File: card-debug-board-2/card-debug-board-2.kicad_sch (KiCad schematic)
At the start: 30 parts, among them J1 2-1734592-0, J2 Conn_01x05, J5 0676430910, J6 629105150521, SW1 PCM13SMTR, SW2 B3F-1000, SW3 CFS-0103TB, SW4 CFS-0103TB, U1 MIC5205-3.3YM5

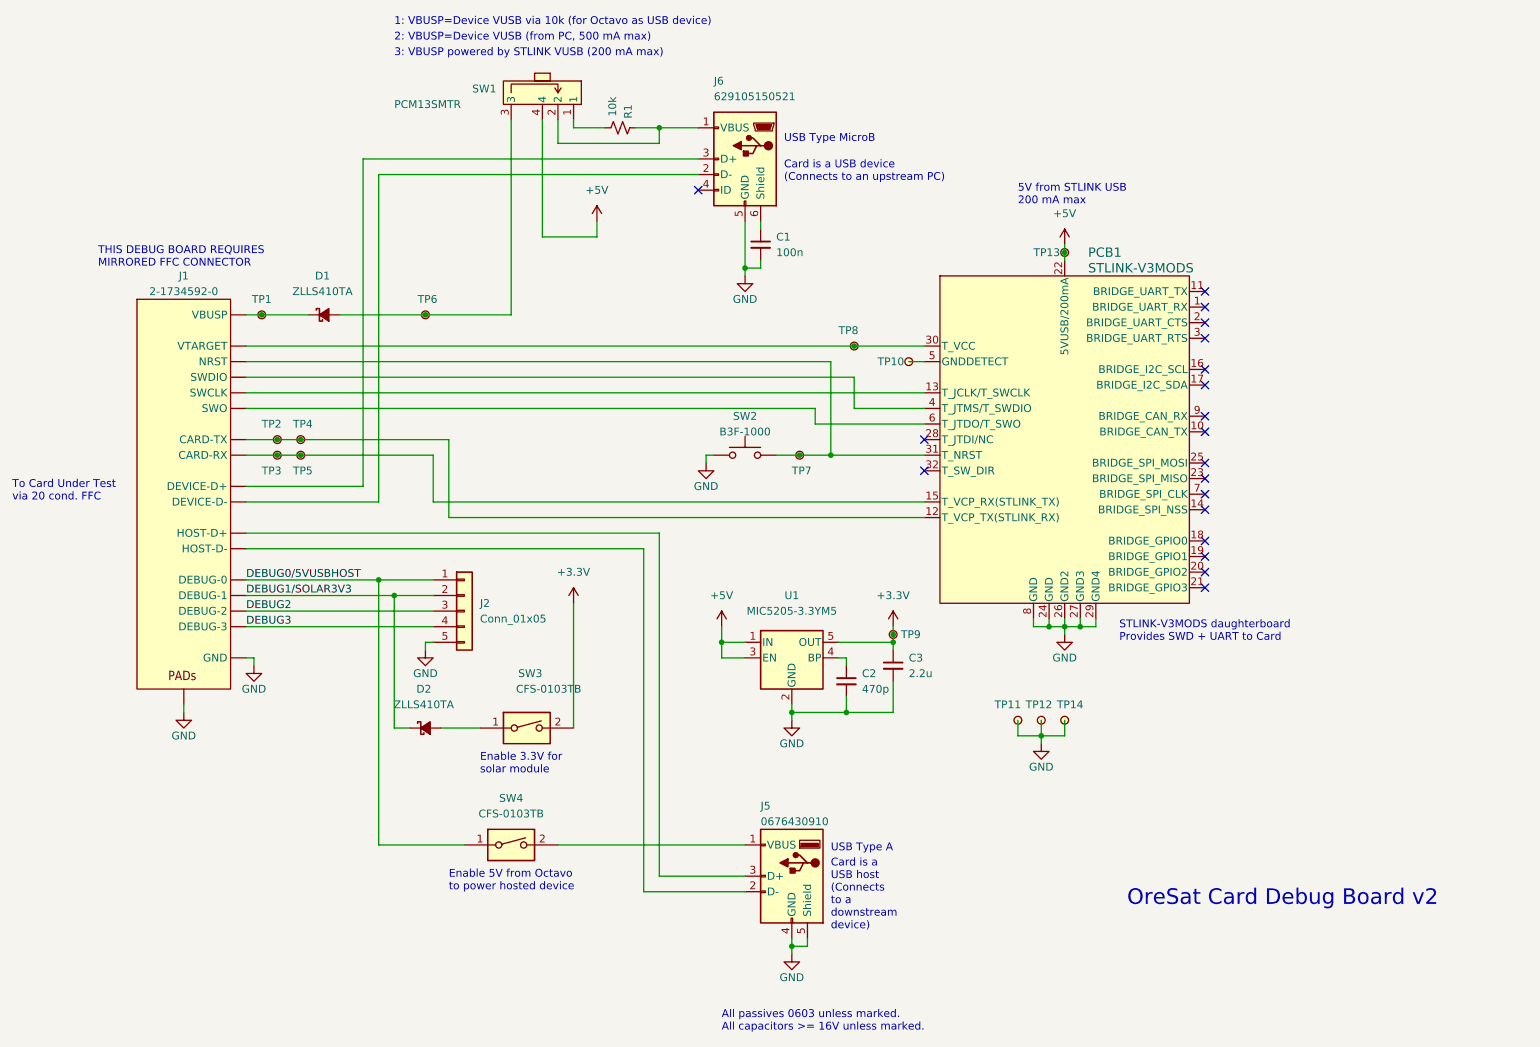
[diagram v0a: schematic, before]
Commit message: Modified debug board, removed several peripherals
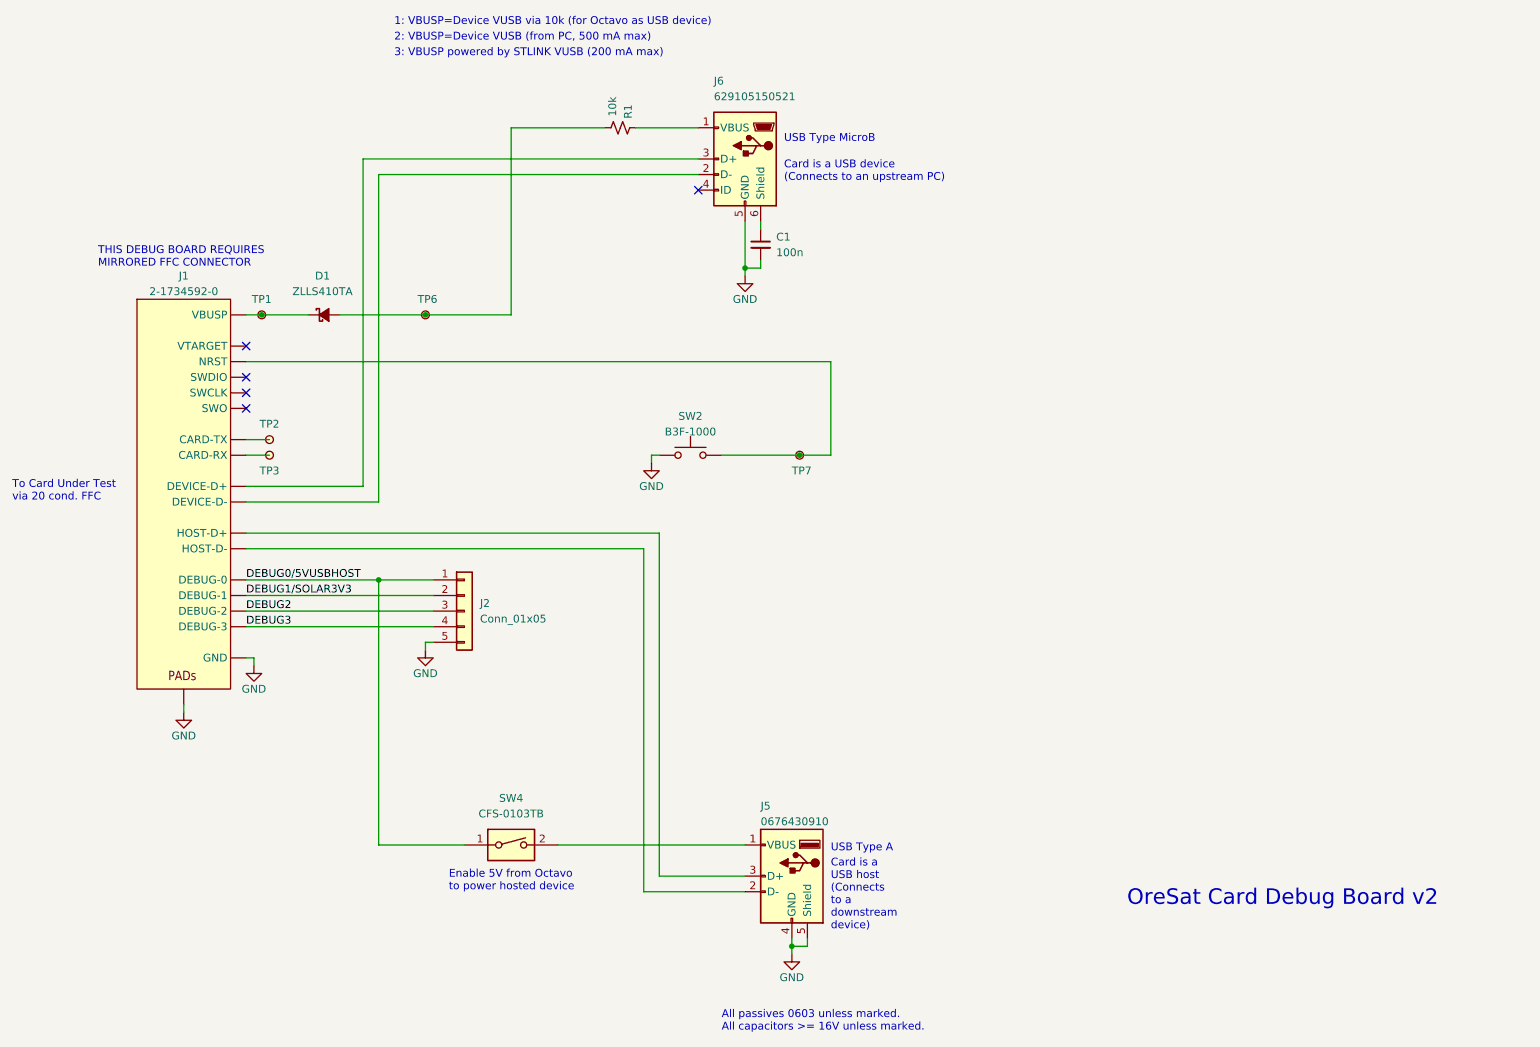
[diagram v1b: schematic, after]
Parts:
- removed C2: 470p, Capacitor_SMD:C_0603_1608Metric, symbol Device:C_Small
- removed C3: 2.2u, Capacitor_SMD:C_0603_1608Metric, symbol Device:C_Small
- removed D2: ZLLS410TA, Diode_SMD:D_SOD-323, symbol Device:D_Schottky_Small_Filled
- removed PCB1: STLINK-V3MODS, oresat-pcbs:STLINK-V3MOS, symbol oresat-pcbs:STLINK-V3MODS
- removed SW1: PCM13SMTR, oresat-misc:SW-CK-PCM13SMTR, symbol oresat-misc:C&K PCM13SMTR
- removed SW3: CFS-0103TB, Button_Switch_SMD:SW_DIP_SPSTx01_Slide_Copal_CHS-01B_W7.62mm_P1.27mm, symbol Switch:SW_DIP_x01
- removed TP10, TP11, TP12, TP13, TP14, TP4, TP5, TP8, TP9: TestPoint-MinTH, oresat-misc:TestPoint-MinTH, symbol oresat-misc:TestPoint-MinTH
- removed U1: MIC5205-3.3YM5, Package_TO_SOT_SMD:SOT-23-5, symbol Regulator_Linear:MIC5205-3.3YM5
- TP2, TP3: footprint oresat-misc:TestPoint-MinTH -> oresat-misc:TestPoint-0.75mm-th
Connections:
- net at D1.2 (A), TP6.1: now also R1.2
- no-connect marks 19 -> 5
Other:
- note removed: "5V from STLINK USB 200 mA max"
- note removed: "Enable 3.3V for solar module"
- note removed: "STLINK-V3MODS daughterboard Provides SWD + UART to Card"
- moved on the sheet: SW2

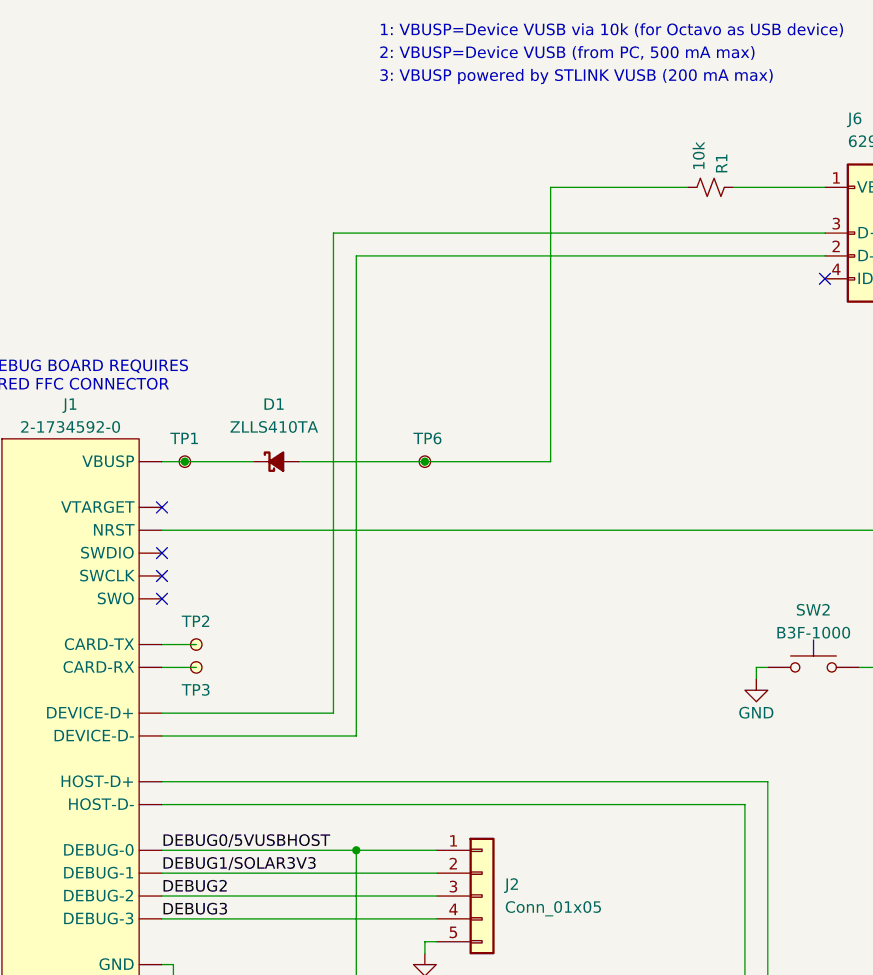
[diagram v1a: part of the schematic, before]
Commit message: Added proper connector for UART and changed 10k ohm resistor on the VBUS line to 0 ohm
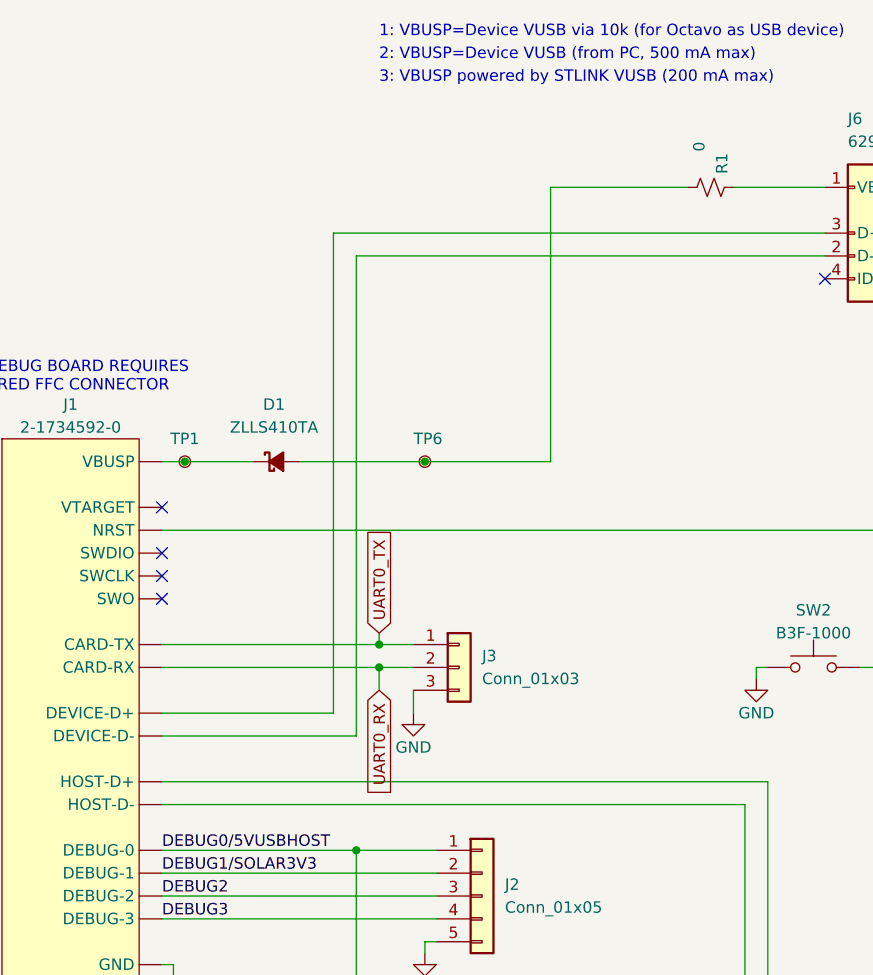
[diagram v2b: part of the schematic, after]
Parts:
- removed TP2, TP3: TestPoint-MinTH, oresat-misc:TestPoint-0.75mm-th, symbol oresat-misc:TestPoint-MinTH
- added J3: Conn_01x03, Connector_PinHeader_2.54mm:PinHeader_1x03_P2.54mm_Vertical, symbol Connector_Generic:Conn_01x03
- J1: value 2-1734592-0 -> 2-1734592-0
- R1: value 10k -> 0
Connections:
- net GND: now also J3.3 (Pin_3)
- net UART0_TX: now reaches J1.13 (CARD-TX)
- net UART0_TX: now also J3.1 (Pin_1)
- net UART0_RX: now reaches J1.12 (CARD-RX)
- net UART0_RX: now also J3.2 (Pin_2)
